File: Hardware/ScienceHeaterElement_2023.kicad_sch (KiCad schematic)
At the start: 8 parts, among them Q1 Si4162DY, U1 LMT85DCK

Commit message: Updated layout for order
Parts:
- D1: footprint (none) -> LED_SMD:LED_0603_1608Metric_Pad1.05x0.95mm_HandSolder
- R1: value 2 -> 7.5; footprint Resistor_SMD:R_0603_1608Metric_Pad0.98x0.95mm_HandSolder -> Package_TO_SOT_THT:TO-126-2_Horizontal_TabDown
- R2: footprint (none) -> Resistor_SMD:R_0603_1608Metric_Pad0.98x0.95mm_HandSolder
- renumbered R4 to R3
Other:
- note added: "Addition Resistance to limit current for the Heater Trace"
- note removed: "Addition Resistance to limit current for the 9.2 Ohm trace"
- moved on the sheet: Conn1, Conn2, R3

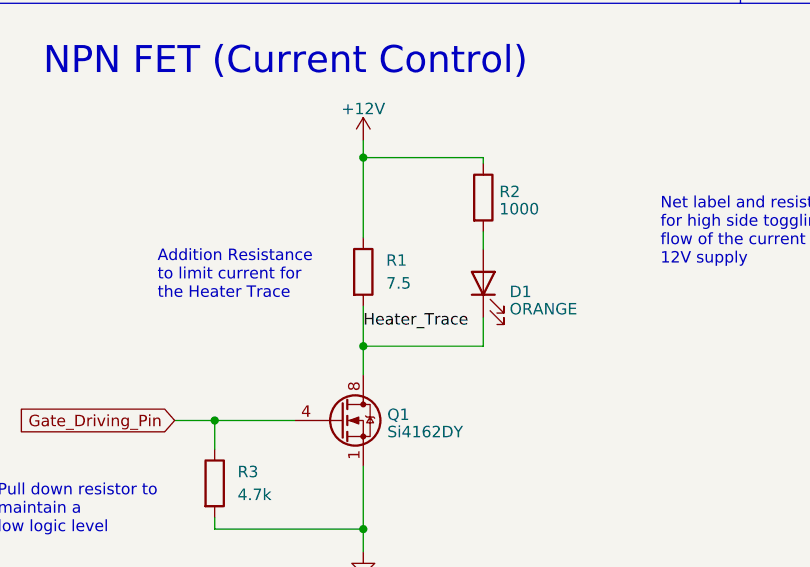
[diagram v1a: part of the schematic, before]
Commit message: Replaced current limiting resistor
Replaced current limiting resistor with 2.5 Ohm resistor and changed the resistor package
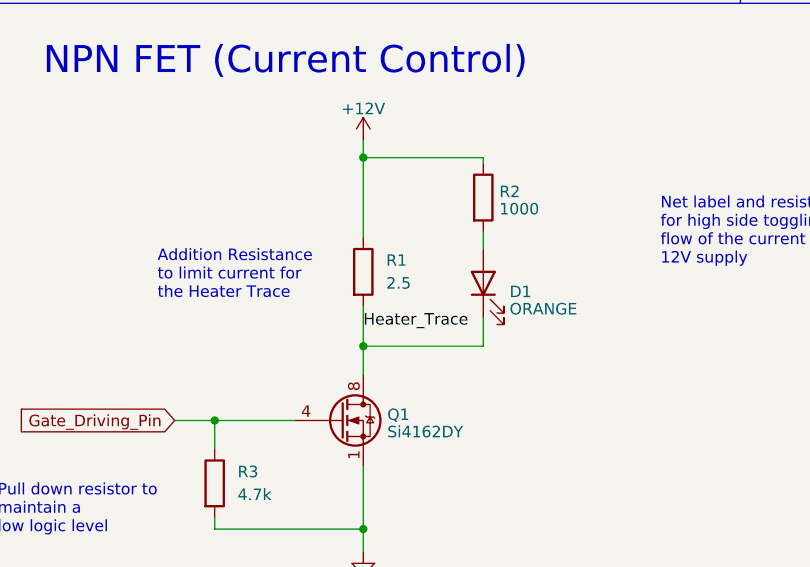
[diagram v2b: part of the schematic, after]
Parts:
- R1: value 7.5 -> 2.5; footprint Package_TO_SOT_THT:TO-126-2_Horizontal_TabDown -> Package_TO_SOT_THT:TO-220-2_Horizontal_TabDown
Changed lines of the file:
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@@
       (effects (font (size 1.27 1.27)) (justify left))
     )
-    (property "Value" "7.5" (at 58.42 95.885 0)
+    (property "Value" "2.5" (at 58.42 95.885 0)
       (effects (font (size 1.27 1.27)) (justify left))
     )
-    (property "Footprint" "Package_TO_SOT_THT:TO-126-2_Horizontal_TabDown" (at 54.102 94.615 90)
+    (property "Footprint" "Package_TO_SOT_THT:TO-220-2_Horizontal_TabDown" (at 54.102 94.615 90)
       (effects (font (size 1.27 1.27)) hide)
     )
